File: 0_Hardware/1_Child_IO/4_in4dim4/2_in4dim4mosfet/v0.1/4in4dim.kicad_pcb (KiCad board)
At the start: 2 copper layers, 100.1 x 86.4 mm, 78 parts, among them IC1 TLP290, J1 RJ45, J2 RJ45, P1 CONN_5, P110 CONN_2, P120 CONN_2, P130 CONN_2, P140 CONN_2, P2 CONN_2, P3 CONN_8X2, Q1 SPP20N60C3, Q2 SPP20N60C3, Q3 SPP20N60C3, Q4 SPP20N60C3, U2 LTV847, U3 LTV847

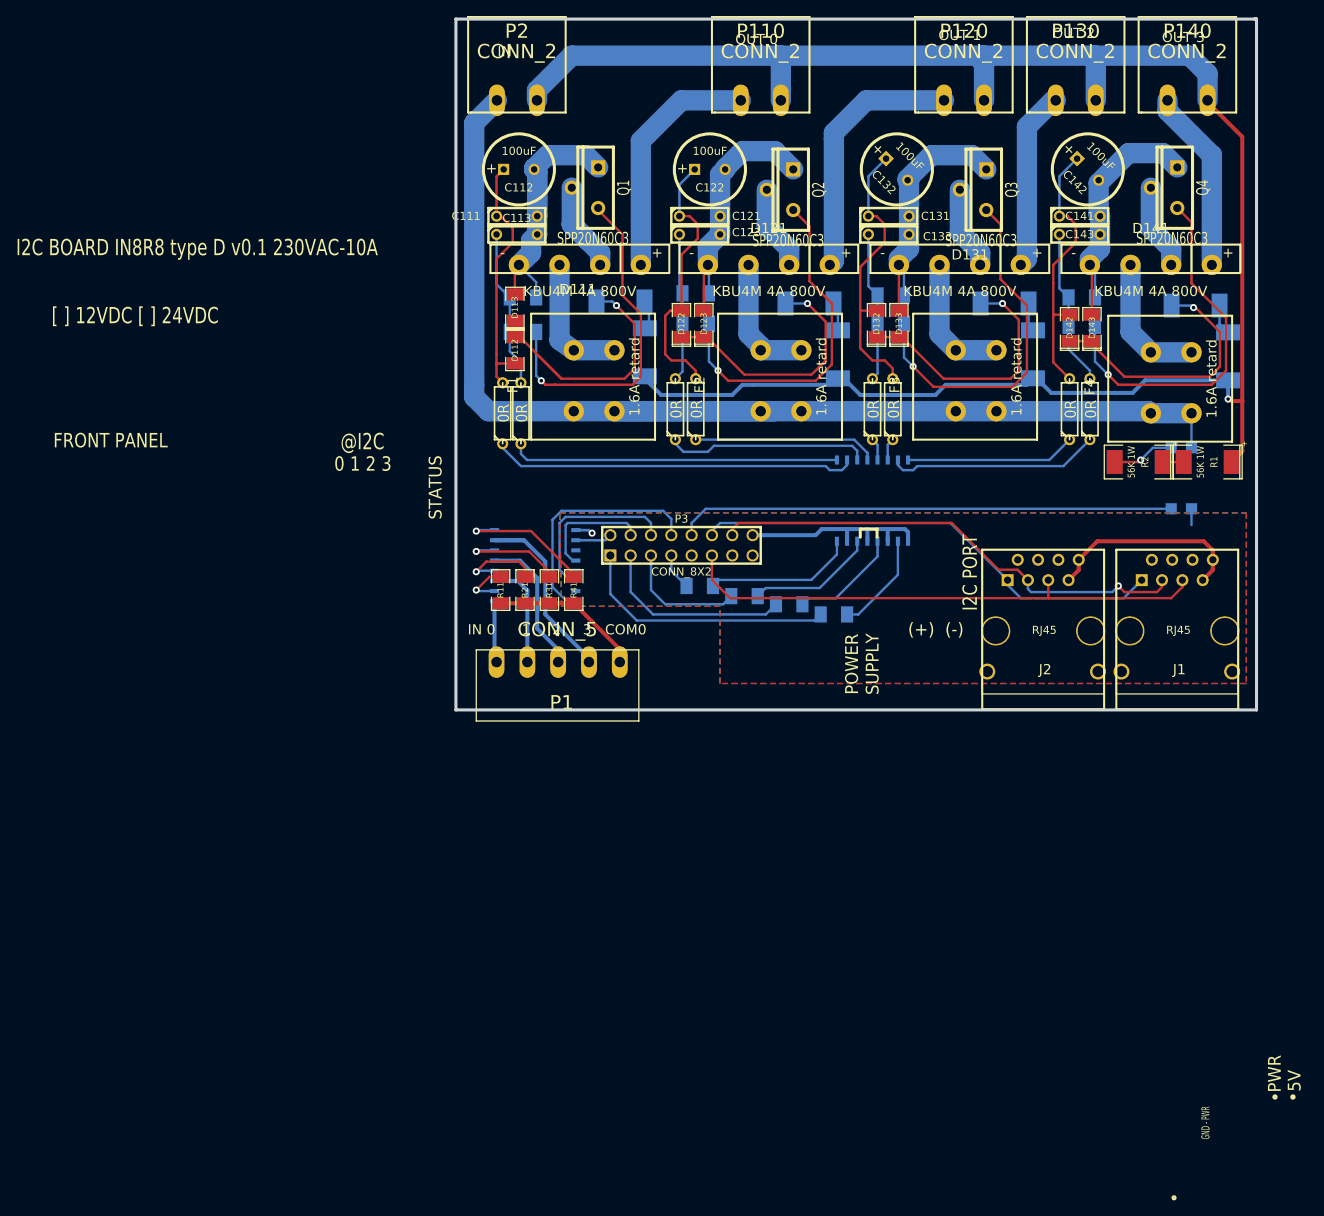
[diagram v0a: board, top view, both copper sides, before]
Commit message: mis à jour de la carte de puissance et de la front panel
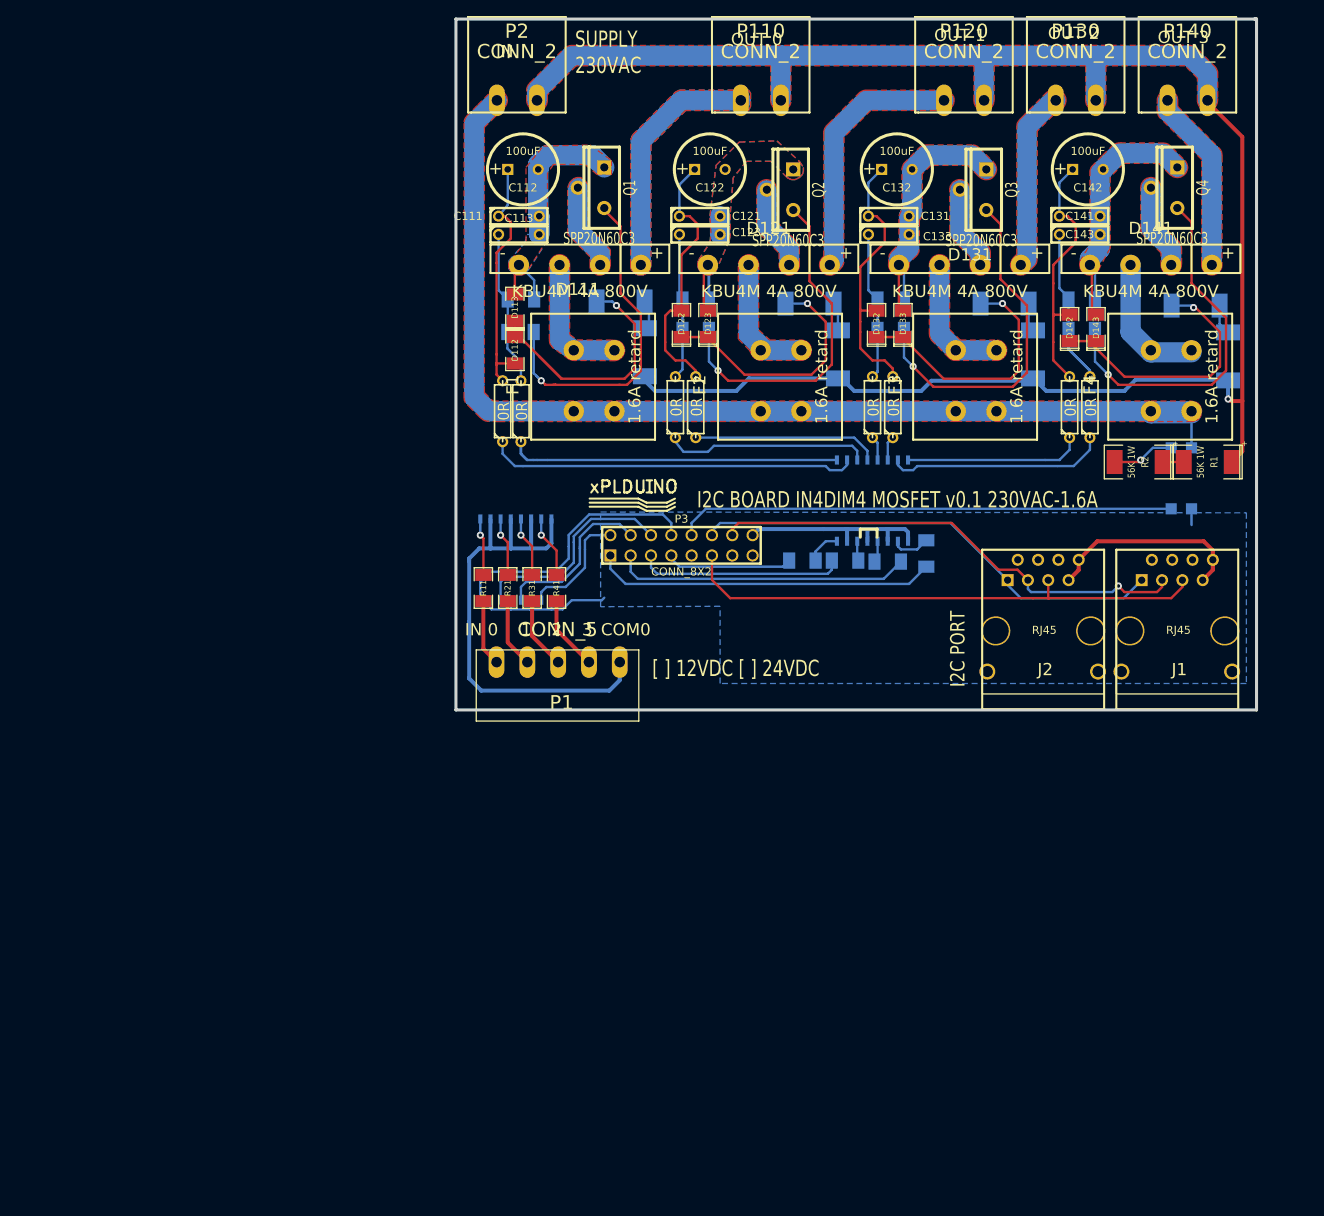
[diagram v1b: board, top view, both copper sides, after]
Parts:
- added logo_xplduino: VAL**, logo_xplduino, F.Cu at (203.7, 131.3)
- moved R16 13.8 mm to (240.4, 137.9), turned to 90 degrees
- moved R17 13.4 mm to (235.6, 138.9), turned to 180 degrees
- moved R18 13.3 mm to (230.3, 138.8)
- moved R19 13.2 mm to (224.9, 138.8)
- moved U2 2.53 mm to (189.1, 138.7), turned to 0 degrees
- moved R11 2.17 mm to (185.0, 142.2)
- moved R21 2.17 mm to (188.1, 142.2)
- moved R31 2.17 mm to (191.1, 142.2)
- moved R41 2.17 mm to (194.2, 142.2)
- moved Q1 0.76 mm to (200.2, 92.2)
- moved R123 0.76 mm to (211.6, 106.2)
- moved R124 0.76 mm to (211.6, 110.0)
- moved R134 0.76 mm to (236.0, 110.0)
- moved D133 0.51 mm to (237.5, 109.2)
- moved R133 0.51 mm to (236.0, 106.2)
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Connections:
- P3 pad 13: N-0000046 -> (no net)
- P3 pad 9: N-0000045 -> (no net)
- R11 pad 1: COM0 -> IN0
- R11 pad 2: N-0000014 -> N-0000066
- R21 pad 1: COM0 -> IN1
- R21 pad 2: N-0000023 (its old number) -> N-0000067
- R31 pad 1: COM0 -> IN2
- R31 pad 2: N-0000022 -> N-0000068
- R41 pad 1: COM0 -> IN3
- R41 pad 2: N-0000021 -> N-0000057
- U2 pad 1: IN0 -> N-0000066
- U2 pad 2: N-0000014 -> COM0
- U2 pad 3: IN1 -> N-0000067
- U2 pad 4: N-0000023 (its old number) -> COM0
- U2 pad 5: IN2 -> N-0000068
- U2 pad 6: N-0000022 -> COM0
- U2 pad 7: IN3 -> N-0000057
- U2 pad 8: N-0000021 -> COM0
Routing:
- net COM0: track 25.0 -> 62.9 mm
- net N-0000021: track 17.1 -> 0.00 mm, vias 1 -> 0
- net IN3: track 26.0 -> 9.29 mm
- net /120S: track 33.2 -> 16.5 mm
- net GND: track 6.41 -> 21.5 mm, vias 1 -> 0
- net N-0000061: track 18.8 -> 4.34 mm
- net N-0000060: track 16.0 -> 2.47 mm
- net N-0000022: track 13.2 -> 0.00 mm, vias 1 -> 0
- net OUT1: track 24.4 -> 37.1 mm
- net OUT3: track 4.60 -> 15.8 mm
- net N-0000059: track 13.8 -> 2.70 mm
- net N-0000023 (its old number): track 10.4 -> 0.00 mm, vias 1 -> 0
- net OUT2: track 15.5 -> 25.8 mm
- net OUT0: track 32.8 -> 42.8 mm
- net CMD3: track 4.58 -> 14.6 mm
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- added copper zone on F.Cu, net /110D
- added copper zone on F.Cu, net /110L
- added copper zone on B.Cu, net /110P
- added copper zone on F.Cu, net /110P
- added copper zone on B.Cu, net /110S
- added copper zone on F.Cu, net /110S
- added copper zone on F.Cu, net /120D
- added copper zone on F.Cu, net /120L
- added copper zone on F.Cu, net /120M
- added copper zone on B.Cu, net /120S
- added copper zone on F.Cu, net /120S
- added copper zone on F.Cu, net /130D
- added copper zone on F.Cu, net /130L
- added copper zone on F.Cu, net /130M
- added copper zone on F.Cu, net /130S
- added copper zone on F.Cu, net /140D
- added copper zone on F.Cu, net /140M
- added copper zone on F.Cu, net /140S
- added copper zone on F.Cu, net L
- added copper zone on F.Cu, net N
- removed copper zone on F.Cu, net GND
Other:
- net class +230V: clearance 0.508 -> 1.016
- board text added: "I2C BOARD IN4DIM4 MOSFET v0.1 230VAC-1.6A"
- board text added: "SUPPLY 230VAC"
- board text removed: "(+) (-)"
- board text removed: "0 1 2 3"
- board text removed: "3 2 1 0 ID 0 0 0 0 0 0 0 0 1 1 0 0 1 0 2 0 0 1 1 3 0 1 0 0 4 0 1 0 1 5 0 1 1 0 6 0 1 1 1 7 1 0 0 0 8 1 0 0 1 9 1 0 1 0 10 1 0 1 1 11 1 1 0 0 12 1 1 0 1 13 1 1 1 0 14 1 1 1 1 15"
- board text removed: "5V"
- board text removed: "@I2C"
- board text removed: "@I2C ID TABLE"
- board text removed: "FRONT PANEL"
- board text removed: "GND - PWR"
- board text removed: "I2C BOARD IN8R8 type D v0.1 230VAC-10A"
- board text removed: "POWER SUPPLY"
- board text removed: "PWR"
- board text removed: "STATUS"

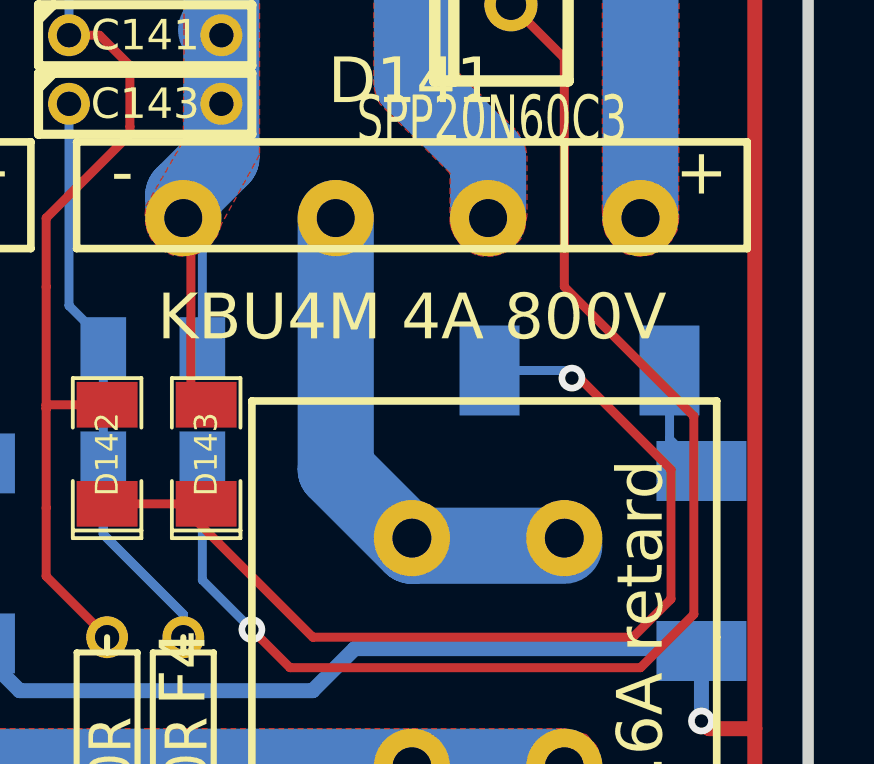
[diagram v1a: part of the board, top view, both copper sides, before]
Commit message: Ajout doublage piste 140M (oubli)
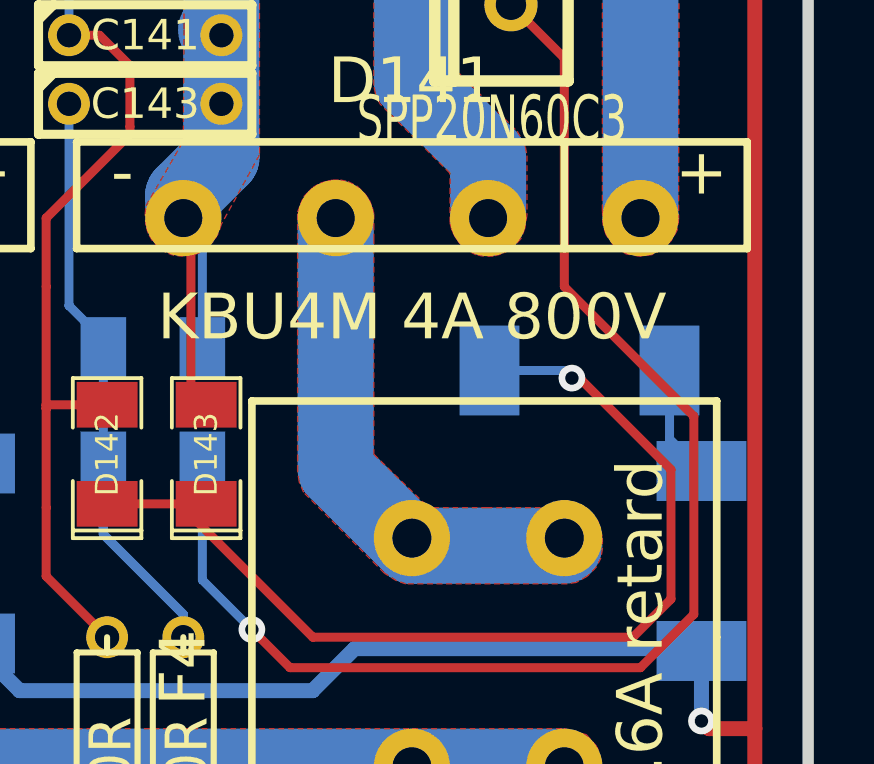
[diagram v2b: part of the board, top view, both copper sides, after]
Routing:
- added copper zone on F.Cu, net /140L
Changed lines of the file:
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@@
     (links 161)
     (no_connects 0)
-    (area 181.419499 70.929499 281.876501 157.670501)
+    (area 172.529499 62.534801 290.322002 169.3672)
     (thickness 1.6002)
     (drawings 68)
@@
       )
     )
+  )
+  (zone (net 15) (net_name /140L) (layer Dessus) (hatch edge 0.508)
+    (connect_pads (clearance 0.254))
+    (min_thickness 0.127)
+    (fill (arc_segments 16) (thermal_gap 0.127) (thermal_bridge_width 1.27))
+    (polygon
+      (pts
+        (xy 273.6596 114.046) (xy 268.2748 114.046) (xy 267.97 113.9444) (xy 267.5636 113.6904) (xy 267.3096 113.4364)
+        (xy 264.8712 110.998) (xy 264.7188 110.6424) (xy 264.668 110.2868) (xy 264.668 109.9312) (xy 264.668 101.9048)
+        (xy 264.668 101.6508) (xy 264.7696 101.3968) (xy 264.8712 101.1428) (xy 265.0236 100.9904) (xy 265.176 100.838)
+        (xy 265.43 100.6856) (xy 265.6332 100.6348) (xy 265.8364 100.584) (xy 266.0904 100.584) (xy 266.3444 100.6348)
+        (xy 266.6492 100.7872) (xy 266.9032 101.0412) (xy 267.0556 101.2444) (xy 267.1572 101.4984) (xy 267.208 101.7016)
+        (xy 267.208 102.0572) (xy 267.208 102.5144) (xy 267.208 109.728) (xy 268.986 111.4552) (xy 269.1892 111.506)
+        (xy 270.9672 111.506) (xy 272.8976 111.506) (xy 274.2184 111.6076) (xy 274.6756 111.9632) (xy 274.828 112.522)
+        (xy 274.828 112.8776) (xy 274.7772 113.1824) (xy 274.6248 113.4872) (xy 274.32 113.792) (xy 273.9644 113.9952)
+      )
+    )

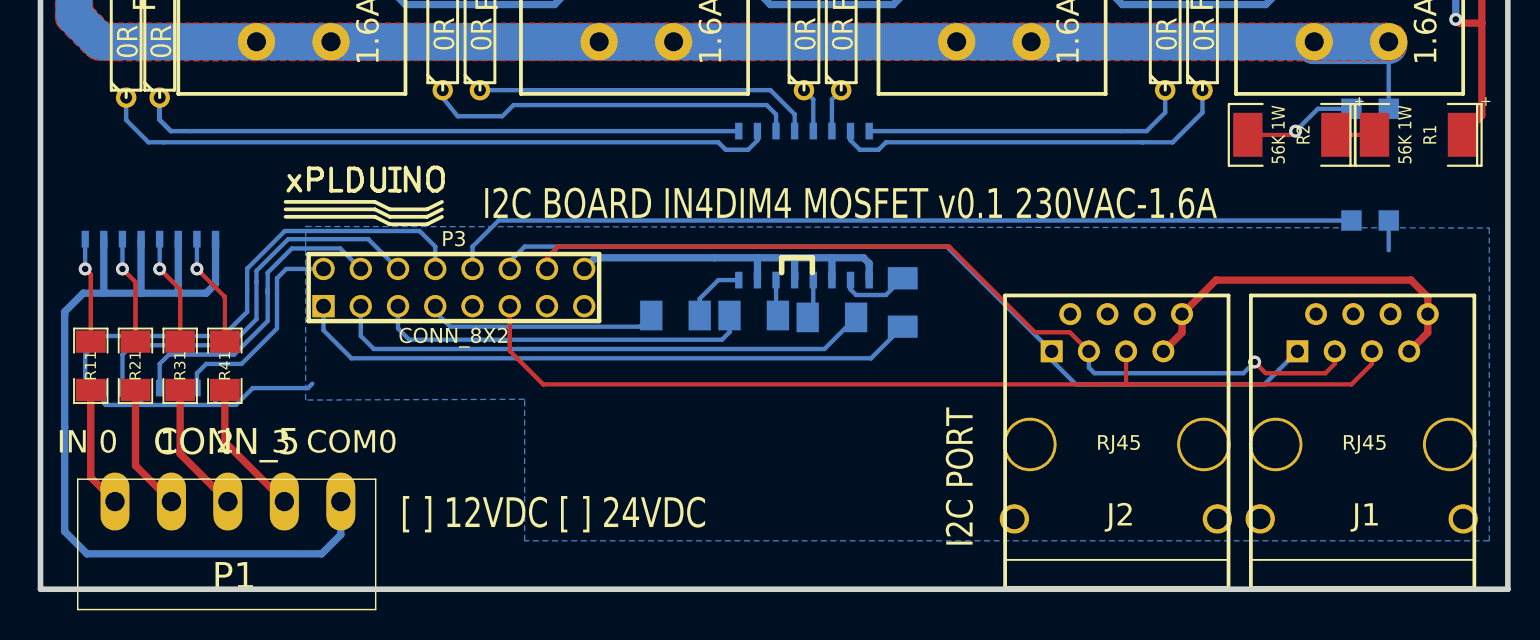
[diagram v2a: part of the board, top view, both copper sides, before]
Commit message: Carte de puissance dimmer - modification du connecteur 20 broches: doublement de 5V et GND et optimisation pinout - modification empreinte des optos 4 canaux et single (création boitier DDIP16 et DDIP4) suite controle des packages des composants - routage pour tenir compte des changements de packages
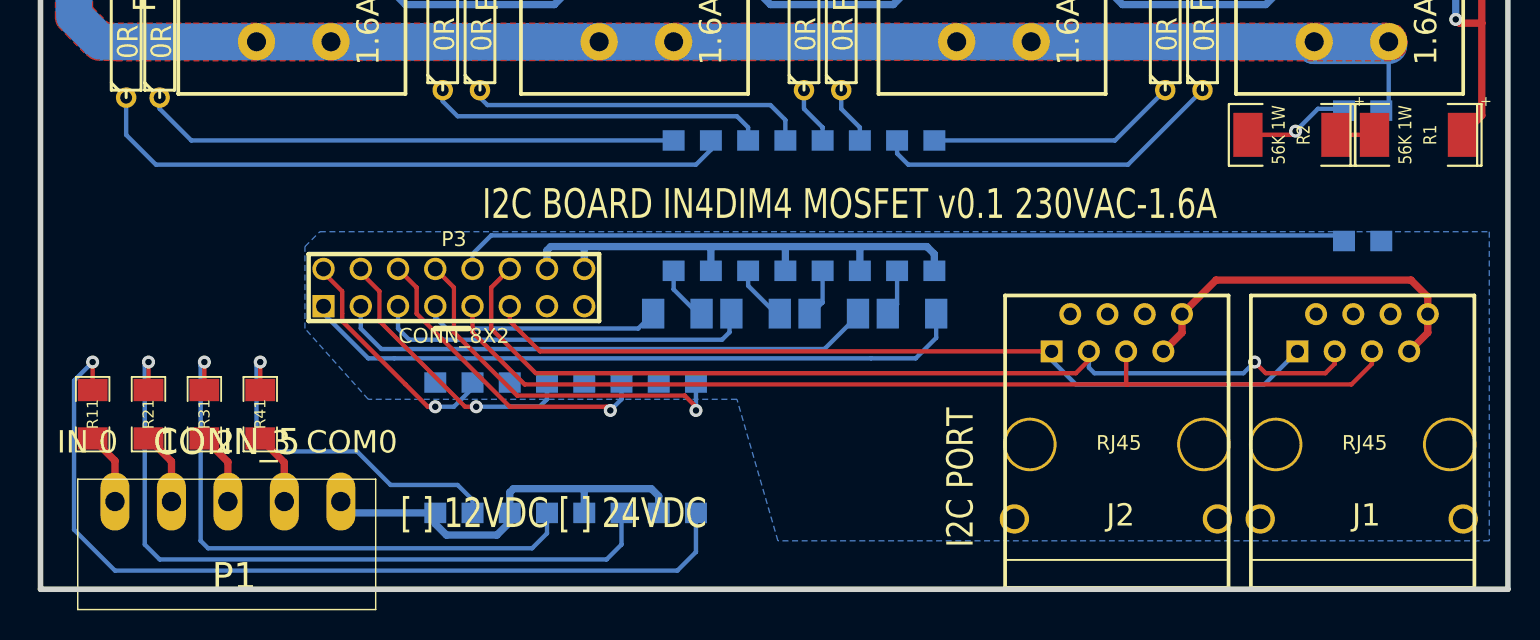
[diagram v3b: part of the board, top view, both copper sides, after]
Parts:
- removed logo_xplduino: VAL**, logo_xplduino
- IC1: footprint SMD-4 -> DDIP-4
- U2, U3: footprint SO16W -> DDIP-16
- moved U2 29.8 mm to (217.4, 147.8), turned to 180 degrees
- moved R41 4.09 mm to (196.6, 145.5)
- moved R31 3.69 mm to (192.8, 145.5)
- moved R21 3.42 mm to (189.0, 145.5)
- moved R11 3.30 mm to (185.2, 145.5)
- moved IC1 1.93 mm to (271.8, 129.3)
- moved R16 0.99 mm to (241.0, 138.7), turned to 180 degrees
- moved R17 0.28 mm to (235.7, 138.7)
- moved R19 0.18 mm to (225.0, 138.7)
- moved R18 0.18 mm to (230.4, 138.7)
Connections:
- P3 pad 11: /INT -> SDA
- P3 pad 12: SDA -> SCL
- P3 pad 13: (no net) -> GND
- P3 pad 14: SCL -> +5V
- P3 pad 9: (no net) -> /INT
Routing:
- net N-0000058: track 7.14 -> 60.6 mm
- net N-0000059: track 7.35 -> 50.0 mm
- net COM0: track 62.9 -> 28.6 mm
- net N-0000060: track 7.56 -> 39.9 mm
- net GND: track 21.5 -> 0.00 mm
- net N-0000061: track 7.77 -> 24.4 mm
- net +5V: track 26.0 -> 35.6 mm
- net CMD0: track 33.3 -> 25.6 mm, vias 0 -> 1
- net N-000008: track 43.9 -> 36.7 mm
- net SCL: track 60.8 -> 67.4 mm
- net CMD1: track 27.1 -> 21.7 mm, vias 0 -> 1
- net N-0000012: track 22.2 -> 17.2 mm
- net IN3: track 9.29 -> 4.99 mm
- net IN2: track 8.96 -> 4.97 mm
- net IN1: track 8.63 -> 4.95 mm
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
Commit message: finalisation dimmer (front et back panel)
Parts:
- added logo_xplduino: VAL**, logo_xplduino, F.Cu at (192.8, 130.3)
- moved R41 3.45 mm to (194.6, 142.7)
- moved R31 3.07 mm to (191.5, 142.7)
- moved R21 2.84 mm to (188.5, 142.7)
- moved R11 2.81 mm to (185.4, 142.7)
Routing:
- net IN2: track 4.97 -> 11.0 mm
- net N-0000061: track 24.4 -> 29.6 mm
- net IN3: track 4.99 -> 8.62 mm
- net N-0000060: track 39.9 -> 43.5 mm
- net N-0000058: track 60.6 -> 64.0 mm
- net N-0000059: track 50.0 -> 53.3 mm
- net IN1: track 4.95 -> 7.96 mm
- net IN0: track 4.94 -> 7.63 mm
- net CMD3: track 16.3 -> 18.1 mm
- net SDA: track 57.8 -> 59.5 mm
- net CMD2: track 19.3 -> 19.9 mm
- added copper zone on F.Cu, net GND
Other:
- board text added: "P - N"
